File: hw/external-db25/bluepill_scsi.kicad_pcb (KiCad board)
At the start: 2 copper layers, 37.3 x 54.1 mm, 11 parts, among them J2 DB25_Male_MountingHoles, J5 Micro_SD_Card, U1 BluePill_STM32F103C

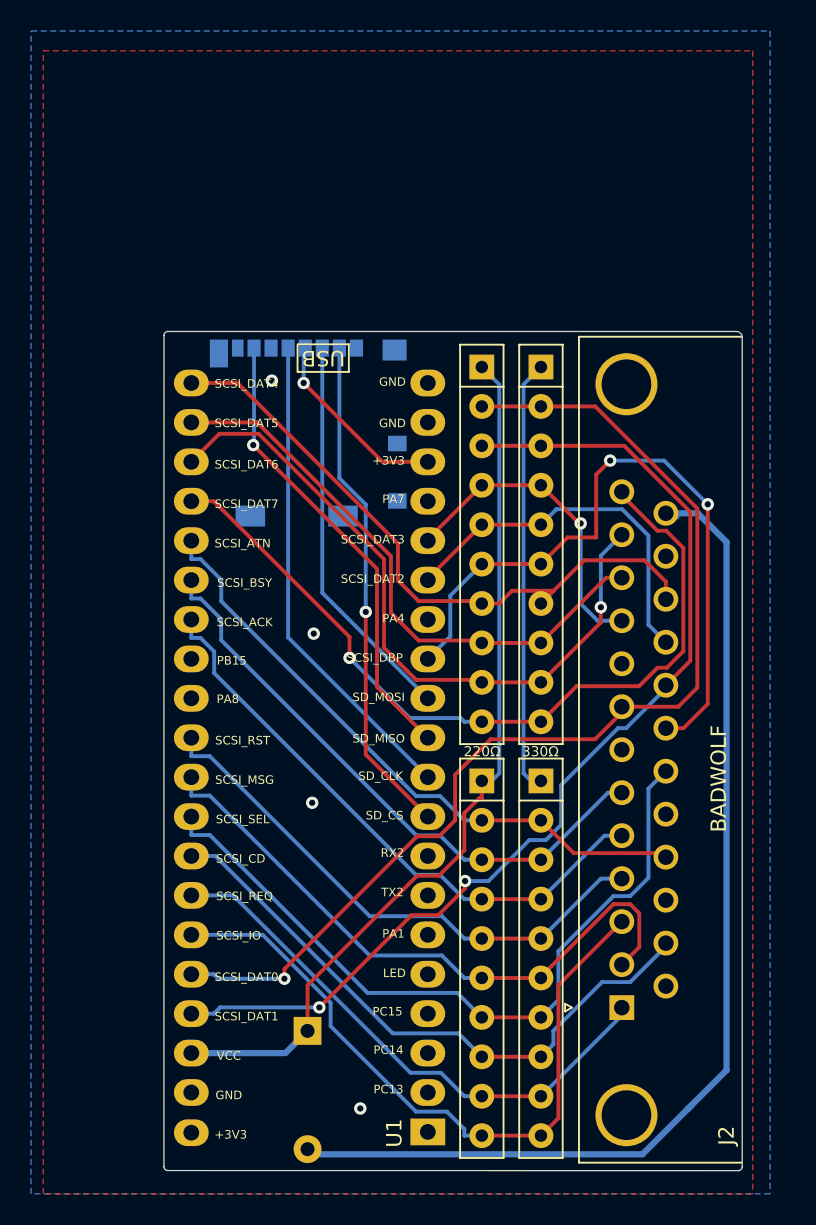
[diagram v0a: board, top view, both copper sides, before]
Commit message: Update footprint to Connector_Dsub:DSUB-25_Male_Horizontal_P2.77x2.84mm_EdgePinOffset7.70mm_Housed_MountingHolesOffset9.12mm to make vertical mounting easier
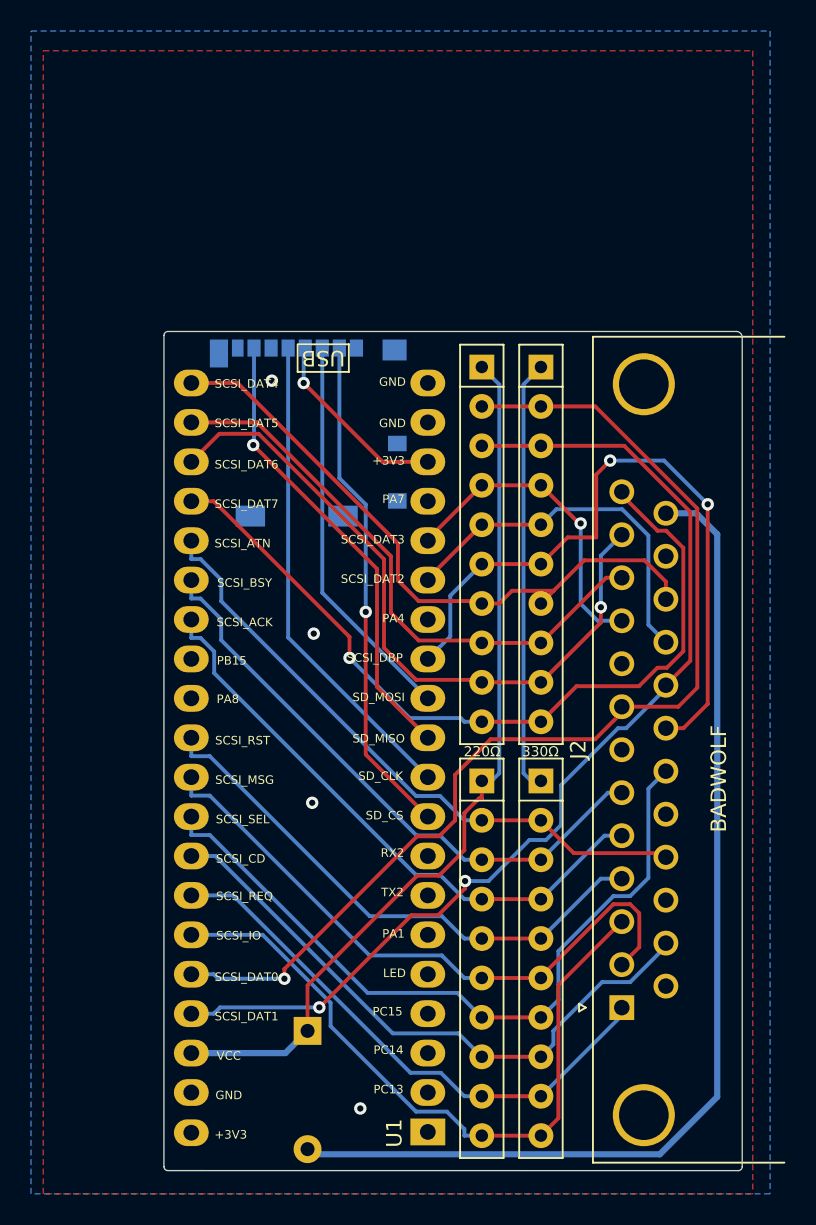
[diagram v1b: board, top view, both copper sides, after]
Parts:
- J2: footprint Connector_Dsub:DSUB-25_Male_Horizontal_P2.77x2.84mm_EdgePinOffset4.94mm_Housed_MountingHolesOffset7.48mm -> Connector_Dsub:DSUB-25_Male_Horizontal_P2.77x2.84mm_EdgePinOffset7.70mm_Housed_MountingHolesOffset9.12mm
